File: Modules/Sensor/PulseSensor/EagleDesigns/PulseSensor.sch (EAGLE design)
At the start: 11 parts, among them U2 ATMEGA328P_TQFP

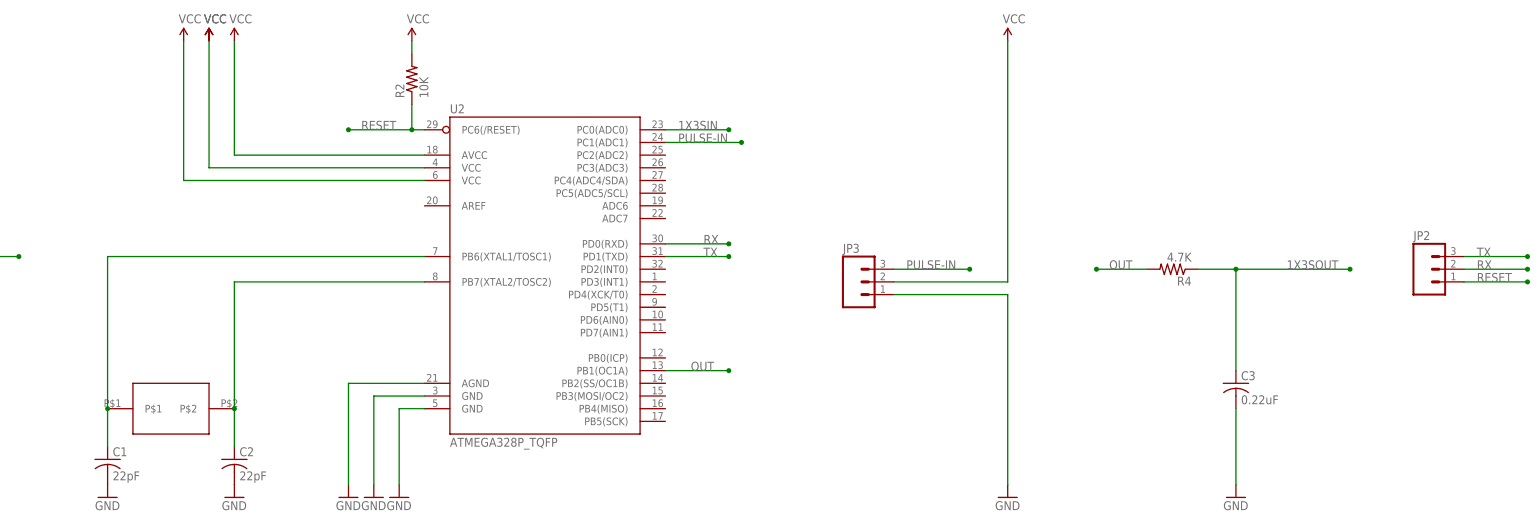
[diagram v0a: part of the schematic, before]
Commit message: PulseSensor: removed crystal, and modified for new bootloader #40
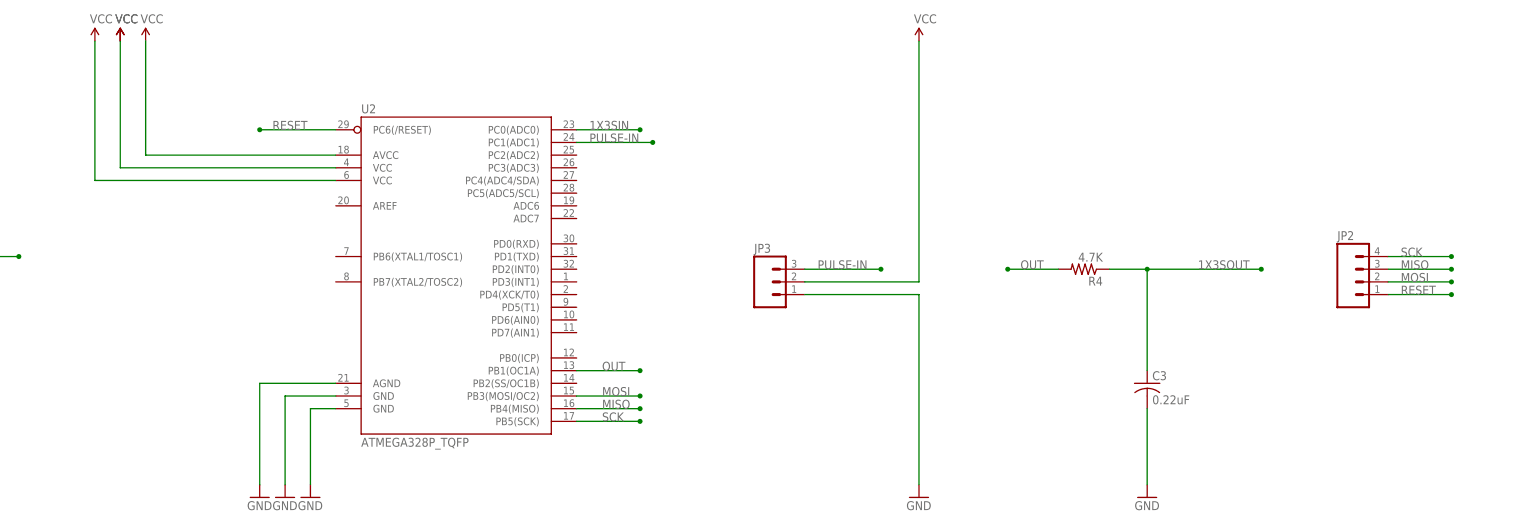
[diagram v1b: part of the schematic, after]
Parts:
- removed C1, C2: 22pF, adafruit:C-USC0603
- removed R2: 10K, resistor:R-US_R0603
- removed U$2: NX503, MakerWear:NX503
- JP2: device SparkFun-Connectors:M03PTH -> SparkFun-Connectors:M04PTH
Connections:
- removed net N$1: C1.1, U$2.P$1, U2.PB6(XTAL1/TOSC1)
- removed net N$3: C2.1, U$2.P$2, U2.PB7(XTAL2/TOSC2)
- removed net RX: JP2.2, U2.PD0(RXD)
- removed net TX: JP2.3, U2.PD1(TXD)
- new net MISO: JP2.3, U2.PB4(MISO)
- new net MOSI: JP2.2, U2.PB3(MOSI/OC2)
- new net SCK: JP2.4, U2.PB5(SCK)
- net GND: no longer C1.2, C2.2
- net RESET: no longer R2.1
- net VCC: no longer R2.2
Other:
- moved on the sheet: C3, JP3, R4, U2
